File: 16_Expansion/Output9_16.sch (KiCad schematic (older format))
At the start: 20 parts, among them J10 String10, J11 String11, J12 String12, J13 String13, J14 String14, J15 String15, J16 String16, J9 String9, U2 SN74HCT245N

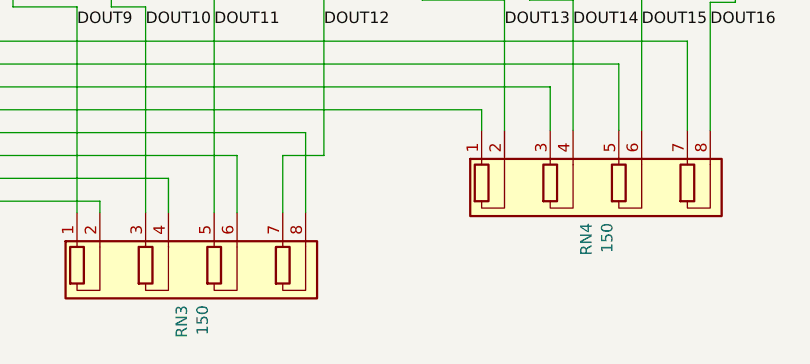
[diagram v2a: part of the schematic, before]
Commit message: Updated Pixel Pixel resistor packs to 33ohms
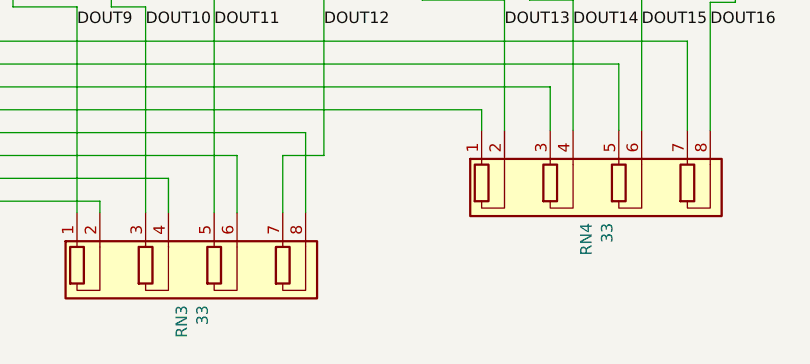
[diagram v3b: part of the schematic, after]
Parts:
- RN3, RN4: value 150 -> 33; Digi-Key_PN 4608X-2-151LF-ND -> 4608X-2-330LF-ND; MPN 4608X-102-151LF -> 4608X-102-330LF
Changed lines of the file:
@@
 AR Path="/5D4698DE/5D4E3AEB" Ref="RN4"  Part="1"
 F 0 "RN4" V 8658 5115 50  0000 L CNN
-F 1 "150" V 8749 5115 50  0000 L CNN
+F 1 "33" V 8749 5115 50  0000 L CNN
 F 2 "Resistor_THT:R_Array_SIP8" V 9375 4910 50  0001 C CNN
 F 3 "http://www.vishay.com/docs/31509/csc.pdf" H 8700 4910 50  0001 C CNN
-F 4 "4608X-2-151LF-ND" H -960 -120 50  0001 C CNN "Digi-Key_PN"
-F 5 "4608X-102-151LF" H -960 -120 50  0001 C CNN "MPN"
+F 4 "4608X-2-330LF-ND" H -960 -120 50  0001 C CNN "Digi-Key_PN"
+F 5 "4608X-102-330LF" H -960 -120 50  0001 C CNN "MPN"
 	1    8700 4910
 	1    0    0    1
@@
 AR Path="/5D4698DE/5D4E3B1E" Ref="RN3"  Part="1"
 F 0 "RN3" V 6888 5475 50  0000 L CNN
-F 1 "150" V 6979 5475 50  0000 L CNN
+F 1 "33" V 6979 5475 50  0000 L CNN
 F 2 "Resistor_THT:R_Array_SIP8" V 7605 5270 50  0001 C CNN
 F 3 "http://www.vishay.com/docs/31509/csc.pdf" H 6930 5270 50  0001 C CNN
-F 4 "4608X-2-151LF-ND" H -760 280 50  0001 C CNN "Digi-Key_PN"
-F 5 "4608X-102-151LF" H -760 280 50  0001 C CNN "MPN"
+F 4 "4608X-2-330LF-ND" H -760 280 50  0001 C CNN "Digi-Key_PN"
+F 5 "4608X-102-330LF" H -760 280 50  0001 C CNN "MPN"
 	1    6930 5270
 	1    0    0    1
